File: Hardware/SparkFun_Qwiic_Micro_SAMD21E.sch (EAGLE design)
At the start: 40 parts, among them Q1 3.1A/30V/105mΩ, U1 3.3V, U2 W25Q32FV, U3 SAMD21E

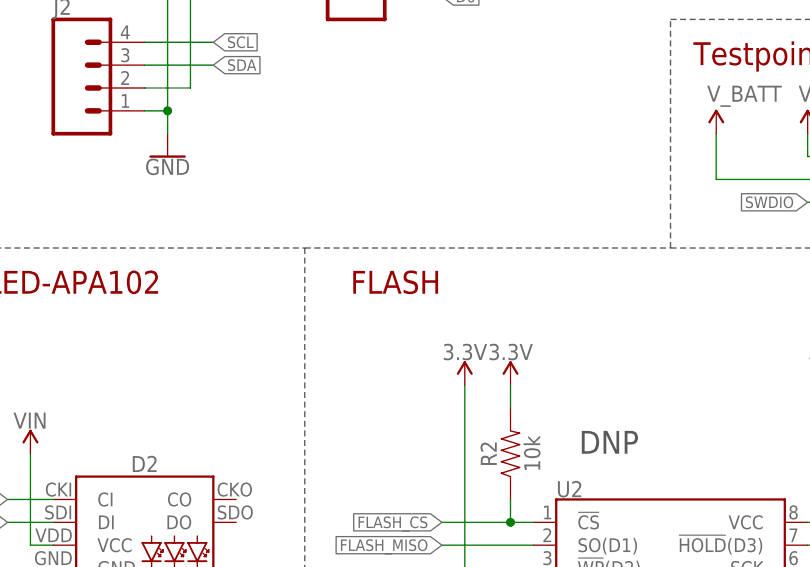
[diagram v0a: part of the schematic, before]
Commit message: Moves some text around
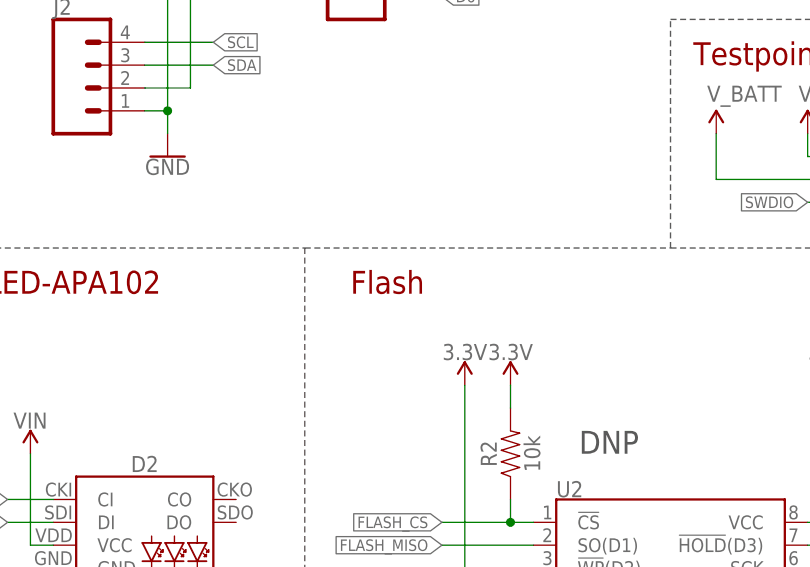
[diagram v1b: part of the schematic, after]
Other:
- note added: "Flash"
- note removed: "FLASH"
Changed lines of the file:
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@@
 <wire x1="144.78" y1="38.1" x2="121.92" y2="38.1" width="0.1524" layer="97" style="shortdash"/>
 <wire x1="48.26" y1="127" x2="48.26" y2="71.12" width="0.1524" layer="97" style="shortdash"/>
-<text x="53.34" y="121.92" size="2.54" layer="94" font="vector">FLASH</text>
+<text x="53.34" y="121.92" size="2.54" layer="94" font="vector">Flash</text>
 <text x="160.02" y="127" size="2.54" layer="97" font="vector">U3</text>
 <text x="68.58" y="43.18" size="1.27" layer="97" font="vector">Cut Jumper

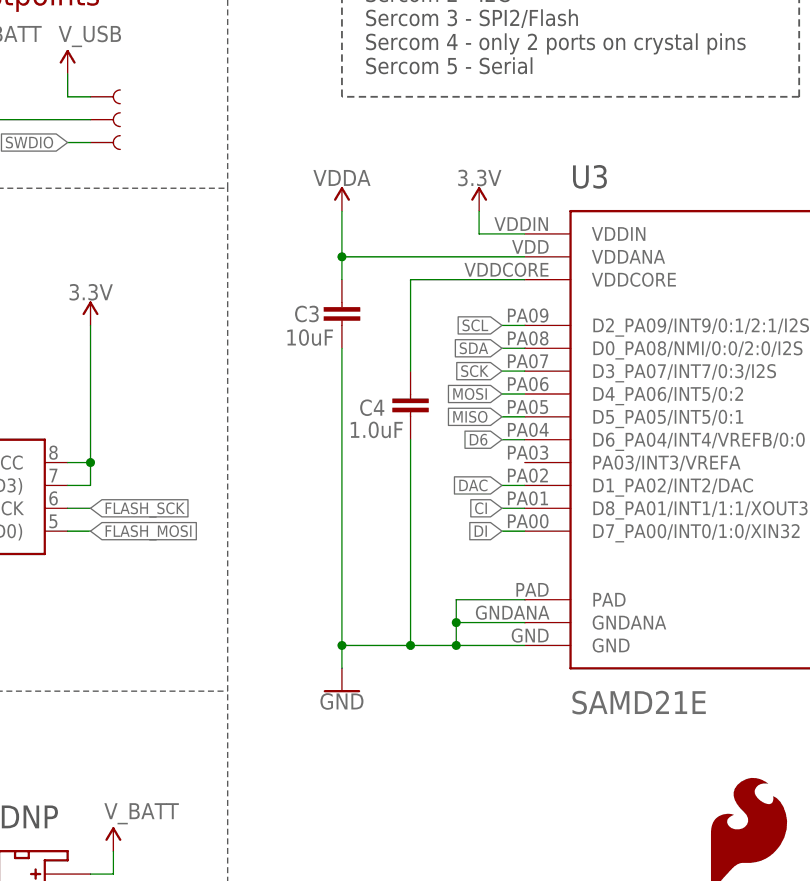
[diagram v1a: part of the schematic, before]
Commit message: Attaches analog voltage pin to 3.3V power rail
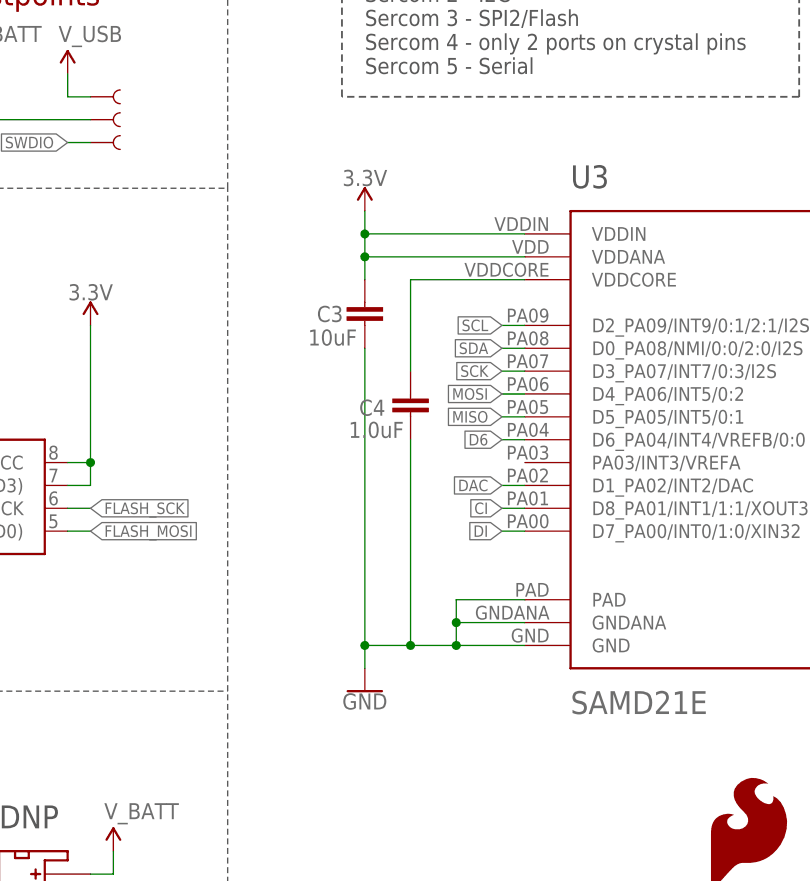
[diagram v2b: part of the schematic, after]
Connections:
- removed net VDDA: C3.1, U3.VDDANA
- net 3.3V: now also C3.1, U3.VDDANA
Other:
- moved on the sheet: C3
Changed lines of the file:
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@@
 <part name="SUPPLY3" library="SparkFun-PowerSymbols" deviceset="V_BATT" device=""/>
 <part name="SUPPLY5" library="SparkFun-PowerSymbols" deviceset="VIN" device=""/>
-<part name="SUPPLY15" library="SparkFun-PowerSymbols" deviceset="VDDA" device=""/>
 <part name="LOGO4" library="SparkFun-Aesthetics" deviceset="QWIIC_LOGO" device="_3MM" value="QWIIC_LOGO_3MM"/>
 <part name="TP3" library="SparkFun-Connectors" deviceset="TEST-POINT" device="TP_15TH_THRU" value="TEST-POINTTP_15TH_THRU"/>
@@
 <attribute name="VALUE" x="29.464" y="26.162" size="1.778" layer="96" font="vector" rot="R180" align="top-center"/>
 </instance>
-<instance part="GND10" gate="1" x="134.62" y="71.12" smashed="yes">
-<attribute name="VALUE" x="134.62" y="70.866" size="1.778" layer="96" font="vector" align="top-center"/>
+<instance part="GND10" gate="1" x="137.16" y="71.12" smashed="yes">
+<attribute name="VALUE" x="137.16" y="70.866" size="1.778" layer="96" font="vector" align="top-center"/>
 </instance>
 <instance part="C4" gate="G$1" x="142.24" y="104.14" smashed="yes" rot="R180">
@@
 <attribute name="VALUE" x="59.944" y="18.161" size="1.778" layer="96" font="vector"/>
 </instance>
-<instance part="SUPPLY16" gate="G$1" x="149.86" y="124.46" smashed="yes">
-<attribute name="VALUE" x="149.86" y="127.254" size="1.778" layer="96" font="vector" align="bottom-center"/>
+<instance part="SUPPLY16" gate="G$1" x="137.16" y="124.46" smashed="yes">
+<attribute name="VALUE" x="137.16" y="127.254" size="1.778" layer="96" font="vector" align="bottom-center"/>
 </instance>
 <instance part="SUPPLY9" gate="G$1" x="83.82" y="50.8" smashed="yes">
@@
 <attribute name="VALUE" x="58.42" y="9.906" size="1.778" layer="96" font="vector" align="top-center"/>
 </instance>
-<instance part="C3" gate="G$1" x="134.62" y="111.76" smashed="yes">
-<attribute name="NAME" x="129.286" y="112.141" size="1.778" layer="95" font="vector"/>
-<attribute name="VALUE" x="128.3064375" y="109.5248" size="1.778" layer="96" font="vector"/>
+<instance part="C3" gate="G$1" x="137.16" y="111.76" smashed="yes">
+<attribute name="NAME" x="131.826" y="112.141" size="1.778" layer="95" font="vector"/>
+<attribute name="VALUE" x="130.8464375" y="109.5248" size="1.778" layer="96" font="vector"/>
 </instance>
 <instance part="C2" gate="G$1" x="66.04" y="20.32" smashed="yes">
@@
 <instance part="SUPPLY5" gate="G$1" x="35.56" y="40.64" smashed="yes">
 <attribute name="VALUE" x="35.56" y="43.434" size="1.778" layer="96" font="vector" align="bottom-center"/>
-</instance>
-<instance part="SUPPLY15" gate="G$1" x="134.62" y="124.46" smashed="yes">
-<attribute name="VALUE" x="134.62" y="127.254" size="1.778" layer="96" font="vector" align="bottom-center"/>
 </instance>
 <instance part="LOGO4" gate="G$1" x="236.22" y="43.18" smashed="yes"/>
@@
 <segment>
 <pinref part="SUPPLY16" gate="G$1" pin="3.3V"/>
-<wire x1="154.94" y1="121.92" x2="149.86" y2="121.92" width="0.1524" layer="91"/>
-<wire x1="149.86" y1="121.92" x2="149.86" y2="124.46" width="0.1524" layer="91"/>
+<wire x1="154.94" y1="121.92" x2="137.16" y2="121.92" width="0.1524" layer="91"/>
+<wire x1="137.16" y1="121.92" x2="137.16" y2="124.46" width="0.1524" layer="91"/>
 <pinref part="U3" gate="G$1" pin="VDDIN"/>
+<pinref part="U3" gate="G$1" pin="VDDANA"/>
+<wire x1="154.94" y1="119.38" x2="137.16" y2="119.38" width="0.1524" layer="91"/>
+<wire x1="137.16" y1="119.38" x2="137.16" y2="121.92" width="0.1524" layer="91"/>
+<junction x="137.16" y="121.92"/>
+<pinref part="C3" gate="G$1" pin="1"/>
+<wire x1="137.16" y1="116.84" x2="137.16" y2="119.38" width="0.1524" layer="91"/>
+<junction x="137.16" y="119.38"/>
 </segment>
 <segment>
@@
 <pinref part="C3" gate="G$1" pin="2"/>
 <wire x1="154.94" y1="78.74" x2="147.32" y2="78.74" width="0.1524" layer="91"/>
-<wire x1="134.62" y1="76.2" x2="134.62" y2="109.22" width="0.1524" layer="91"/>
+<wire x1="137.16" y1="76.2" x2="137.16" y2="109.22" width="0.1524" layer="91"/>
 <wire x1="154.94" y1="76.2" x2="147.32" y2="76.2" width="0.1524" layer="91"/>
 <wire x1="154.94" y1="81.28" x2="147.32" y2="81.28" width="0.1524" layer="91"/>
 <wire x1="147.32" y1="81.28" x2="147.32" y2="78.74" width="0.1524" layer="91"/>
-<wire x1="142.24" y1="76.2" x2="134.62" y2="76.2" width="0.1524" layer="91"/>
+<wire x1="142.24" y1="76.2" x2="137.16" y2="76.2" width="0.1524" layer="91"/>
 <wire x1="142.24" y1="76.2" x2="147.32" y2="76.2" width="0.1524" layer="91"/>
 <wire x1="147.32" y1="78.74" x2="147.32" y2="76.2" width="0.1524" layer="91"/>
@@
 <junction x="147.32" y="76.2"/>
 <pinref part="GND10" gate="1" pin="GND"/>
-<wire x1="134.62" y1="73.66" x2="134.62" y2="76.2" width="0.1524" layer="91"/>
-<junction x="134.62" y="76.2"/>
+<wire x1="137.16" y1="73.66" x2="137.16" y2="76.2" width="0.1524" layer="91"/>
+<junction x="137.16" y="76.2"/>
 <pinref part="U3" gate="G$1" pin="GNDANA"/>
 <pinref part="U3" gate="G$1" pin="GND"/>
@@
 </segment>
 </net>
-<net name="VDDA" class="0">
-<segment>
-<wire x1="154.94" y1="119.38" x2="134.62" y2="119.38" width="0.1524" layer="91"/>
-<pinref part="C3" gate="G$1" pin="1"/>
-<wire x1="134.62" y1="119.38" x2="134.62" y2="116.84" width="0.1524" layer="91"/>
-<pinref part="SUPPLY15" gate="G$1" pin="VDDA"/>
-<wire x1="134.62" y1="119.38" x2="134.62" y2="124.46" width="0.1524" layer="91"/>
-<junction x="134.62" y="119.38"/>
-<pinref part="U3" gate="G$1" pin="VDDANA"/>
-</segment>
-</net>

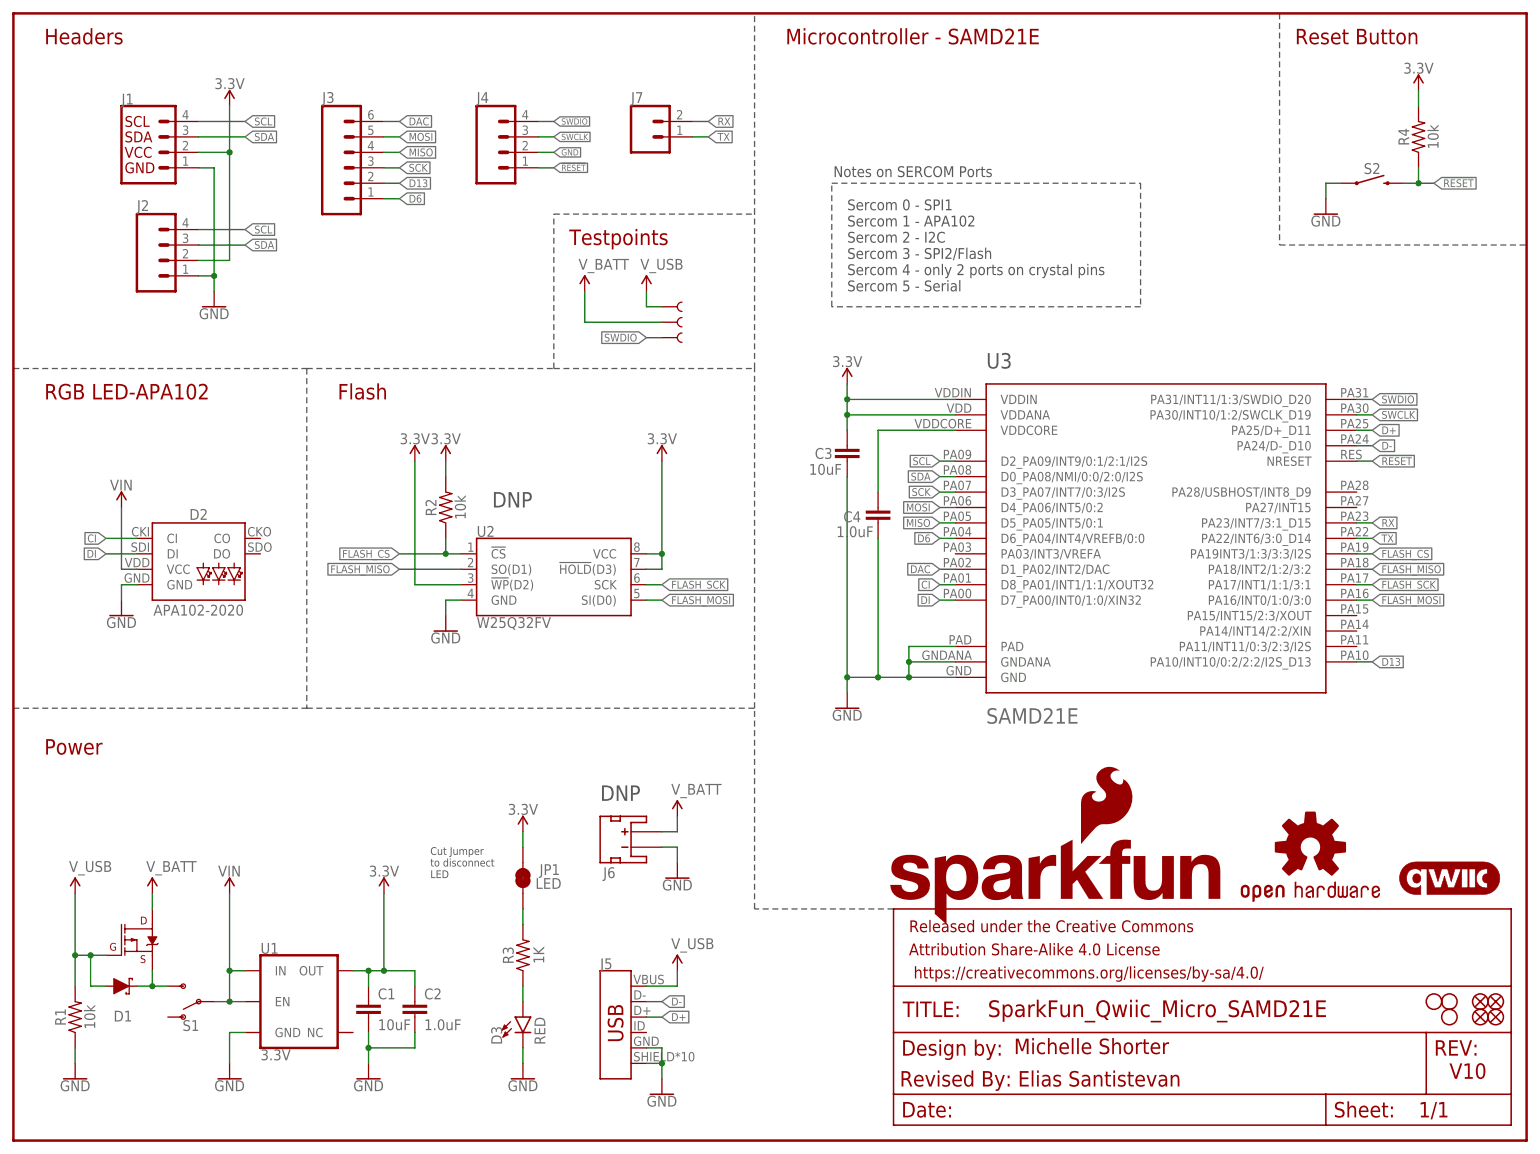
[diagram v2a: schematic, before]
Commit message: Updates numbering on samd21E
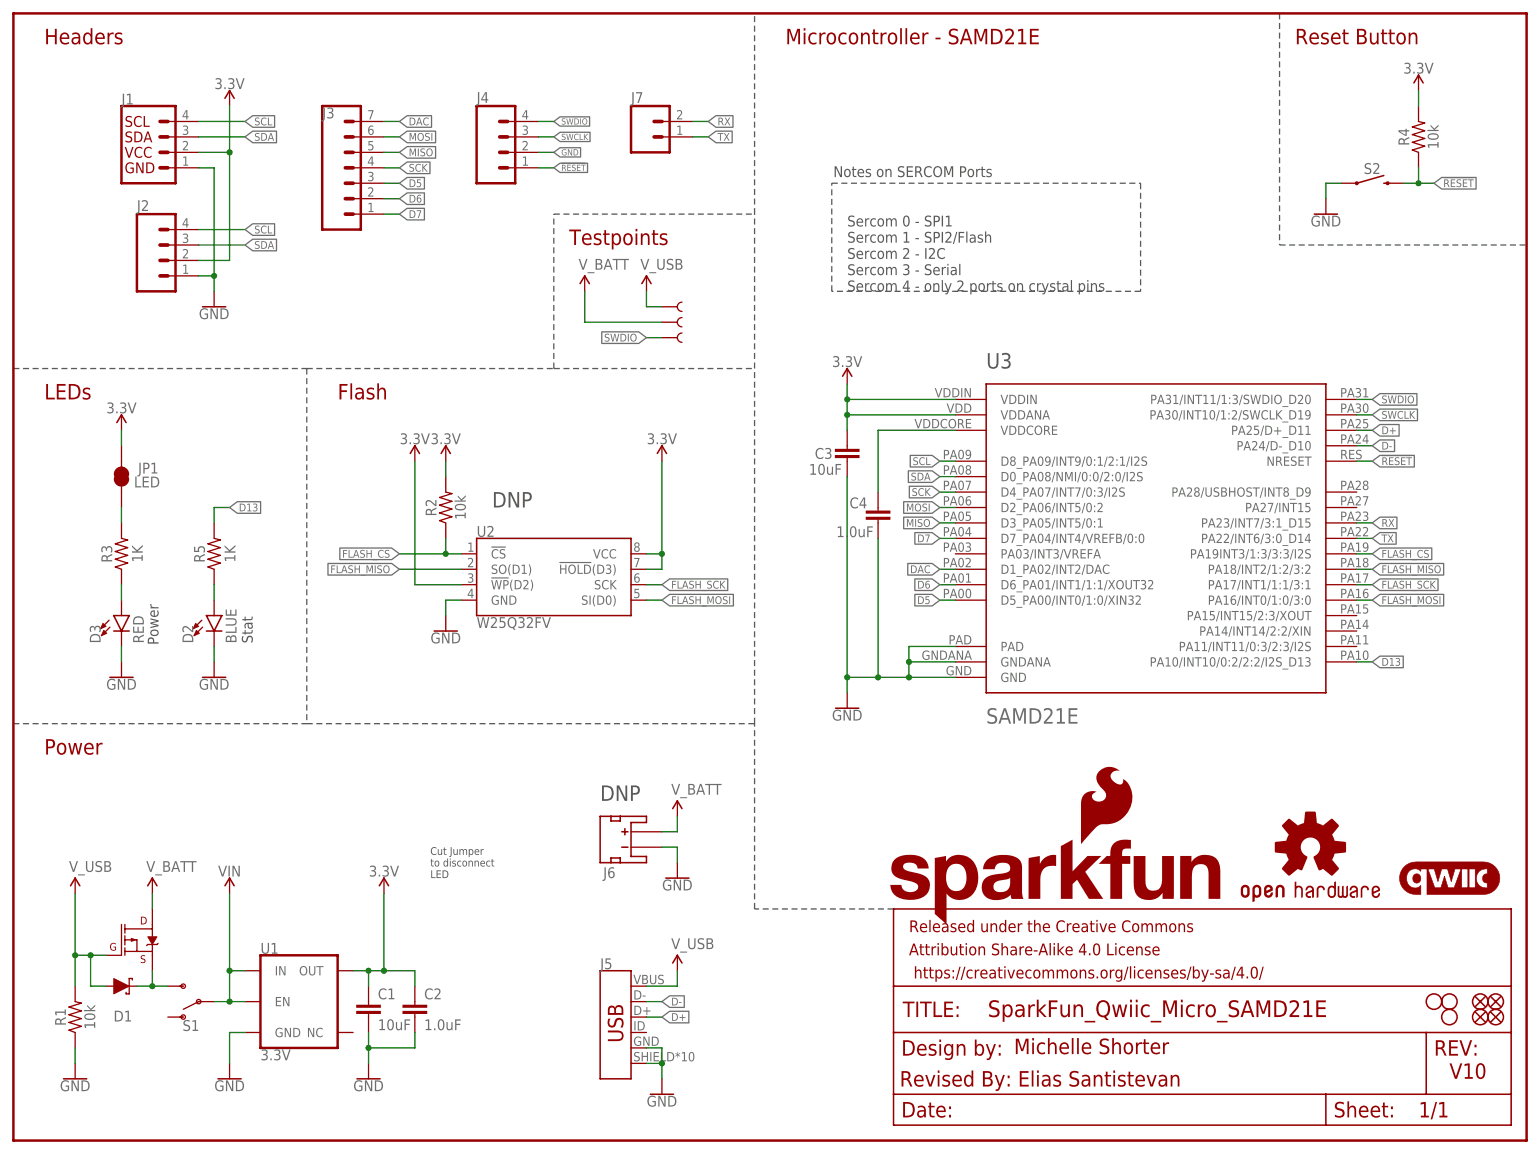
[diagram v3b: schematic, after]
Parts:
- added R5: 1K, SparkFun-Resistors:1KOHM-0402-1/16W-1%
- D2: value APA102-2020 -> BLUE; device SparkFun-LED:APA102-2020 -> SparkFun-LED:LED-BLUE0603
- J3: device SparkFun-Connectors:CONN_06NO_SILK_NO_POP -> SparkFun-Connectors:CONN_07NO_SILK
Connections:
- removed net CI: D2.CI, U3.D8_PA01/INT1/1:1/XOUT32
- removed net DI: D2.DI, U3.D7_PA00/INT0/1:0/XIN32
- new net D5: J3.3, U3.D5_PA00/INT0/1:0/XIN32
- new net D7: J3.1, U3.D7_PA04/INT4/VREFB/0:0
- new net N$4: D2.A, R5.1
- net D13: now also R5.2; no longer J3.2
- net D6: now also J3.2, U3.D6_PA01/INT1/1:1/XOUT32; no longer J3.1, U3.D6_PA04/INT4/VREFB/0:0
- net DAC: now also J3.7; no longer J3.6
- net GND: now also D2.C; no longer D2.GND
- net MISO: now also J3.5, U3.D3_PA05/INT5/0:1; no longer J3.4, U3.D5_PA05/INT5/0:1
- net MOSI: now also J3.6, U3.D2_PA06/INT5/0:2; no longer J3.5, U3.D4_PA06/INT5/0:2
- net SCK: now also J3.4, U3.D4_PA07/INT7/0:3/I2S; no longer J3.3, U3.D3_PA07/INT7/0:3/I2S
- net SCL: now also U3.D8_PA09/INT9/0:1/2:1/I2S; no longer U3.D2_PA09/INT9/0:1/2:1/I2S
- net VIN: no longer D2.VCC
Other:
- note added: "LEDs"
- note added: "Sercom 0 - SPI1 Sercom 1 - SPI2/Flash Sercom 2 - I2C Sercom 3 - Serial Sercom 4 - only 2 ports on crystal pins"
- note added: "Stat"
- note removed: "RGB LED-APA102"
- note removed: "Sercom 0 - SPI1 Sercom 1 - APA102 Sercom 2 - I2C Sercom 3 - SPI2/Flash Sercom 4 - only 2 ports on crystal pins Sercom 5 - Serial"
- moved on the sheet: D3, JP1, R3

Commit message: Huge update
* Changes pin layout in arduino files which are now reflected in SAMD21 symbol
* reroutes different lines to the headers on the left side of the board
* removes the APA102 in favor of blue stat LED
* Changes Qwiic Micro Arduino pin order and internal APA102 pin assignments
* Adds gerbers
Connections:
- net D+: now also U3.PA25/D+_D32; no longer U3.PA25/D+_D11
- net D-: now also U3.PA24/D-_D31; no longer U3.PA24/D-_D10
- net RX: now also U3.PA23/INT7/3:1_D17; no longer U3.PA23/INT7/3:1_D15
- net SWCLK: now also U3.PA30/INT10/1:2/SWCLK_D22; no longer U3.PA30/INT10/1:2/SWCLK_D19
- net SWDIO: now also U3.PA31/INT11/1:3/SWDIO_D23; no longer U3.PA31/INT11/1:3/SWDIO_D20
- net TX: now also U3.PA22/INT6/3:0_D16; no longer U3.PA22/INT6/3:0_D14
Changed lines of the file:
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@@
 <wire x1="220.98" y1="121.92" x2="223.52" y2="121.92" width="0.1524" layer="91"/>
 <label x="223.52" y="121.92" size="1.27" layer="95" font="vector" xref="yes"/>
-<pinref part="U3" gate="G$1" pin="PA31/INT11/1:3/SWDIO_D20"/>
+<pinref part="U3" gate="G$1" pin="PA31/INT11/1:3/SWDIO_D23"/>
 </segment>
 <segment>
@@
 <wire x1="220.98" y1="119.38" x2="223.52" y2="119.38" width="0.1524" layer="91"/>
 <label x="223.52" y="119.38" size="1.27" layer="95" font="vector" xref="yes"/>
-<pinref part="U3" gate="G$1" pin="PA30/INT10/1:2/SWCLK_D19"/>
+<pinref part="U3" gate="G$1" pin="PA30/INT10/1:2/SWCLK_D22"/>
 </segment>
 <segment>
@@
 <wire x1="220.98" y1="116.84" x2="223.52" y2="116.84" width="0.1524" layer="91"/>
 <label x="223.52" y="116.84" size="1.27" layer="95" font="vector" xref="yes"/>
-<pinref part="U3" gate="G$1" pin="PA25/D+_D11"/>
+<pinref part="U3" gate="G$1" pin="PA25/D+_D32"/>
 </segment>
 <segment>
@@
 <wire x1="220.98" y1="114.3" x2="223.52" y2="114.3" width="0.1524" layer="91"/>
 <label x="223.52" y="114.3" size="1.27" layer="95" font="vector" xref="yes"/>
-<pinref part="U3" gate="G$1" pin="PA24/D-_D10"/>
+<pinref part="U3" gate="G$1" pin="PA24/D-_D31"/>
 </segment>
 <segment>
@@
 <wire x1="220.98" y1="101.6" x2="223.52" y2="101.6" width="0.1524" layer="91"/>
 <label x="223.52" y="101.6" size="1.27" layer="95" font="vector" xref="yes"/>
-<pinref part="U3" gate="G$1" pin="PA23/INT7/3:1_D15"/>
+<pinref part="U3" gate="G$1" pin="PA23/INT7/3:1_D17"/>
 </segment>
 </net>
@@
 <wire x1="220.98" y1="99.06" x2="223.52" y2="99.06" width="0.1524" layer="91"/>
 <label x="223.52" y="99.06" size="1.27" layer="95" font="vector" xref="yes"/>
-<pinref part="U3" gate="G$1" pin="PA22/INT6/3:0_D14"/>
+<pinref part="U3" gate="G$1" pin="PA22/INT6/3:0_D16"/>
 </segment>
 </net>
